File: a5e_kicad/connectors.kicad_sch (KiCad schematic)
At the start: 0 parts

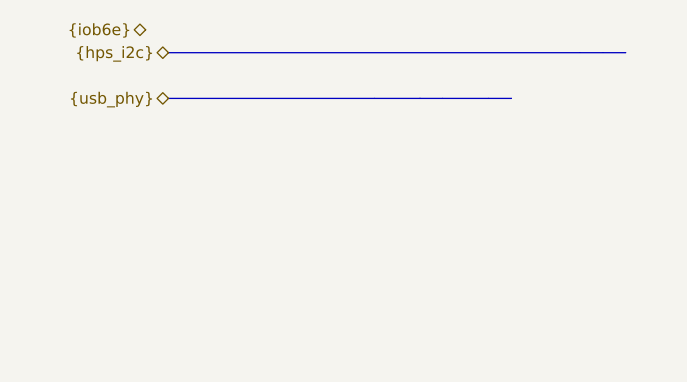
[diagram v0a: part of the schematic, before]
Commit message: Remove unused USB leftovers
USB is not used on this board.
- HPS sheet: remove the {hps_usb} ULPI bus, labels and wires; the 12
  U7 USB0 pins get no-connect flags
- Connectors sheet: remove the {usb_phy} hierarchical label and bus
- Clock sheet: remove the unused clk4 (USB 24 MHz) outputs and note
- Top-level: remove the {hps_usb}, {usb_phy}, clk4_P/clk4_N sheet pins
  and the usb_clk24 net

Netlist compared before/after: only the 12 USB pin nets changed (now
unconnected). ERC 542 -> 522.
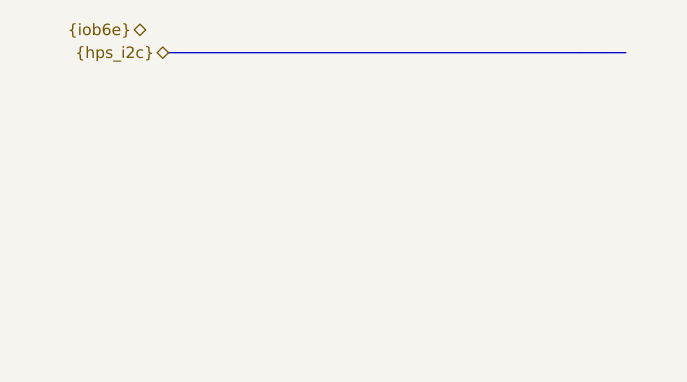
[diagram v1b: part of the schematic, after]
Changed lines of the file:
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@@
-	(bus
-		(pts
-			(xy 30.48 22.86) (xy 53.34 22.86)
-		)
-		(stroke
-			(width 0)
-			(type default)
-		)
-	)
 	(bus
 		(pts
@@
 	(bus
 		(pts
-			(xy 53.34 22.86) (xy 58.42 22.86)
-		)
-		(stroke
-			(width 0)
-			(type default)
-		)
-	)
-	(bus
-		(pts
 			(xy 35.56 134.62) (xy 35.56 193.04)
 		)
@@
 	(bus
 		(pts
-			(xy 60.96 22.86) (xy 66.04 22.86)
-		)
-		(stroke
-			(width 0)
-			(type default)
-		)
-	)
-	(bus
-		(pts
 			(xy 71.12 193.04) (xy 73.66 193.04)
 		)
@@
 	(bus
 		(pts
-			(xy 66.04 22.86) (xy 68.58 22.86)
-		)
-		(stroke
-			(width 0)
-			(type default)
-		)
-	)
-	(bus
-		(pts
 			(xy 266.7 129.54) (xy 269.24 129.54)
 		)
@@
 		(pts
 			(xy 93.98 193.04) (xy 96.52 193.04)
-		)
-		(stroke
-			(width 0)
-			(type default)
-		)
-	)
-	(bus
-		(pts
-			(xy 58.42 22.86) (xy 60.96 22.86)
 		)
 		(stroke
@@
 		(effects
 			(font
-				(size 1.27 1.27)
-			)
-			(justify right)
-		)
-	)
-	(hierarchical_label "{usb_phy}"
-		(shape bidirectional)
-		(at 30.48 22.86 180)
-		(effects
-			(font

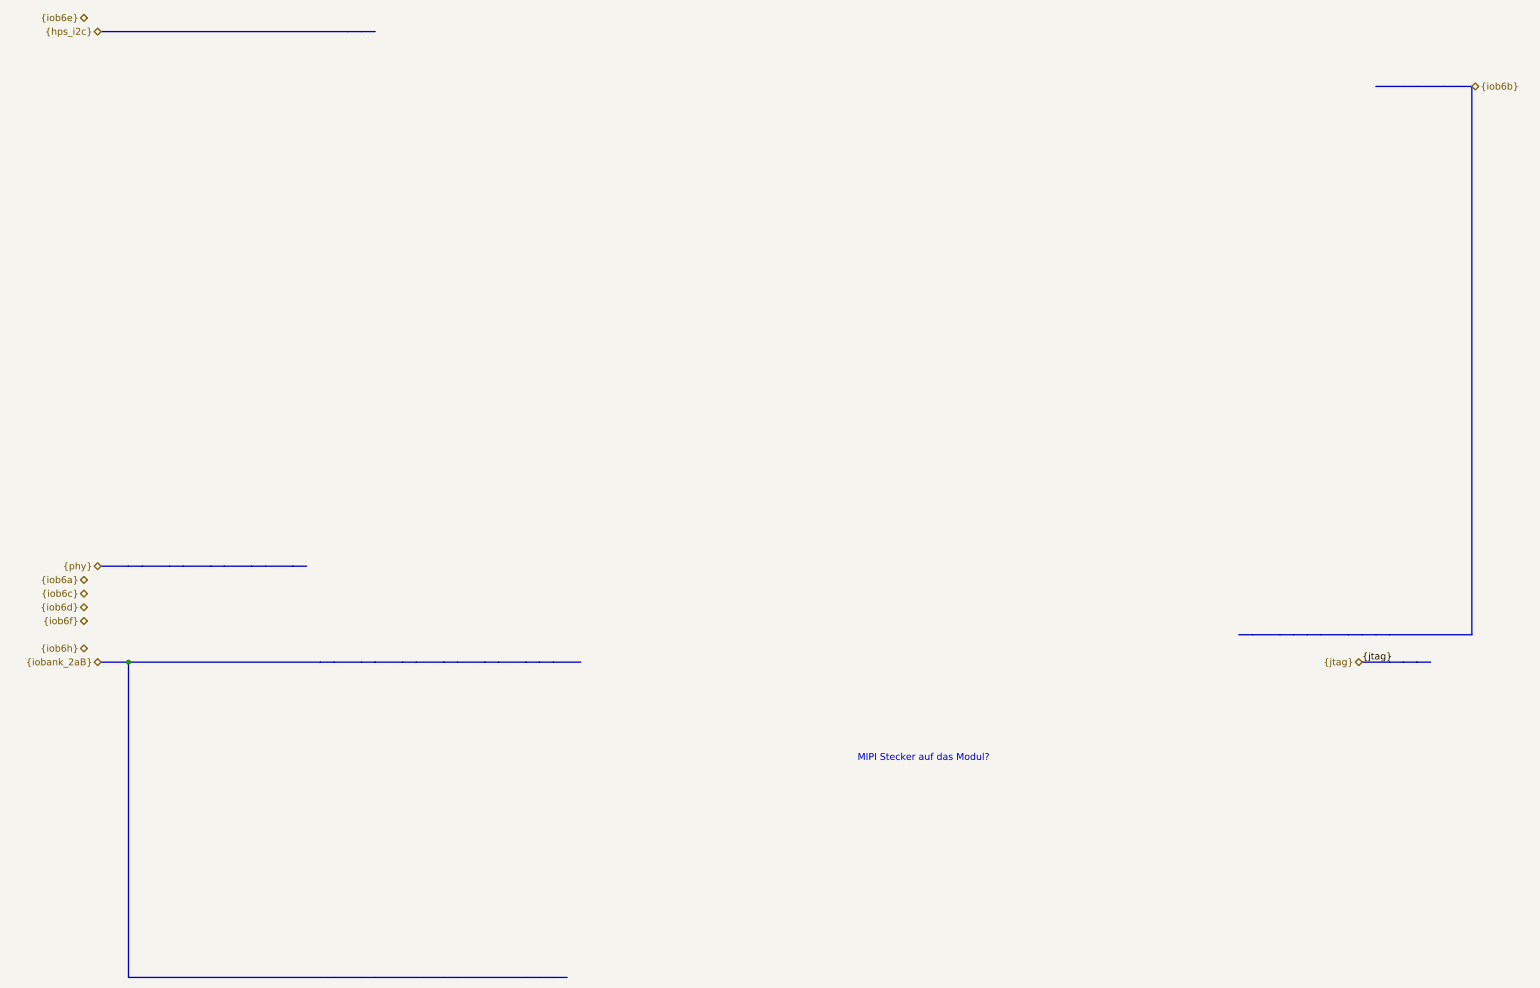
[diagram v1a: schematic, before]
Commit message: Update PCB from schematic
Sync net names after the P1/P2/USB cleanup (schematic parity 142 -> 0).
KiCad also dropped the empty leftover buses on the connectors sheet and
re-serialized instance data. Netlist unchanged.
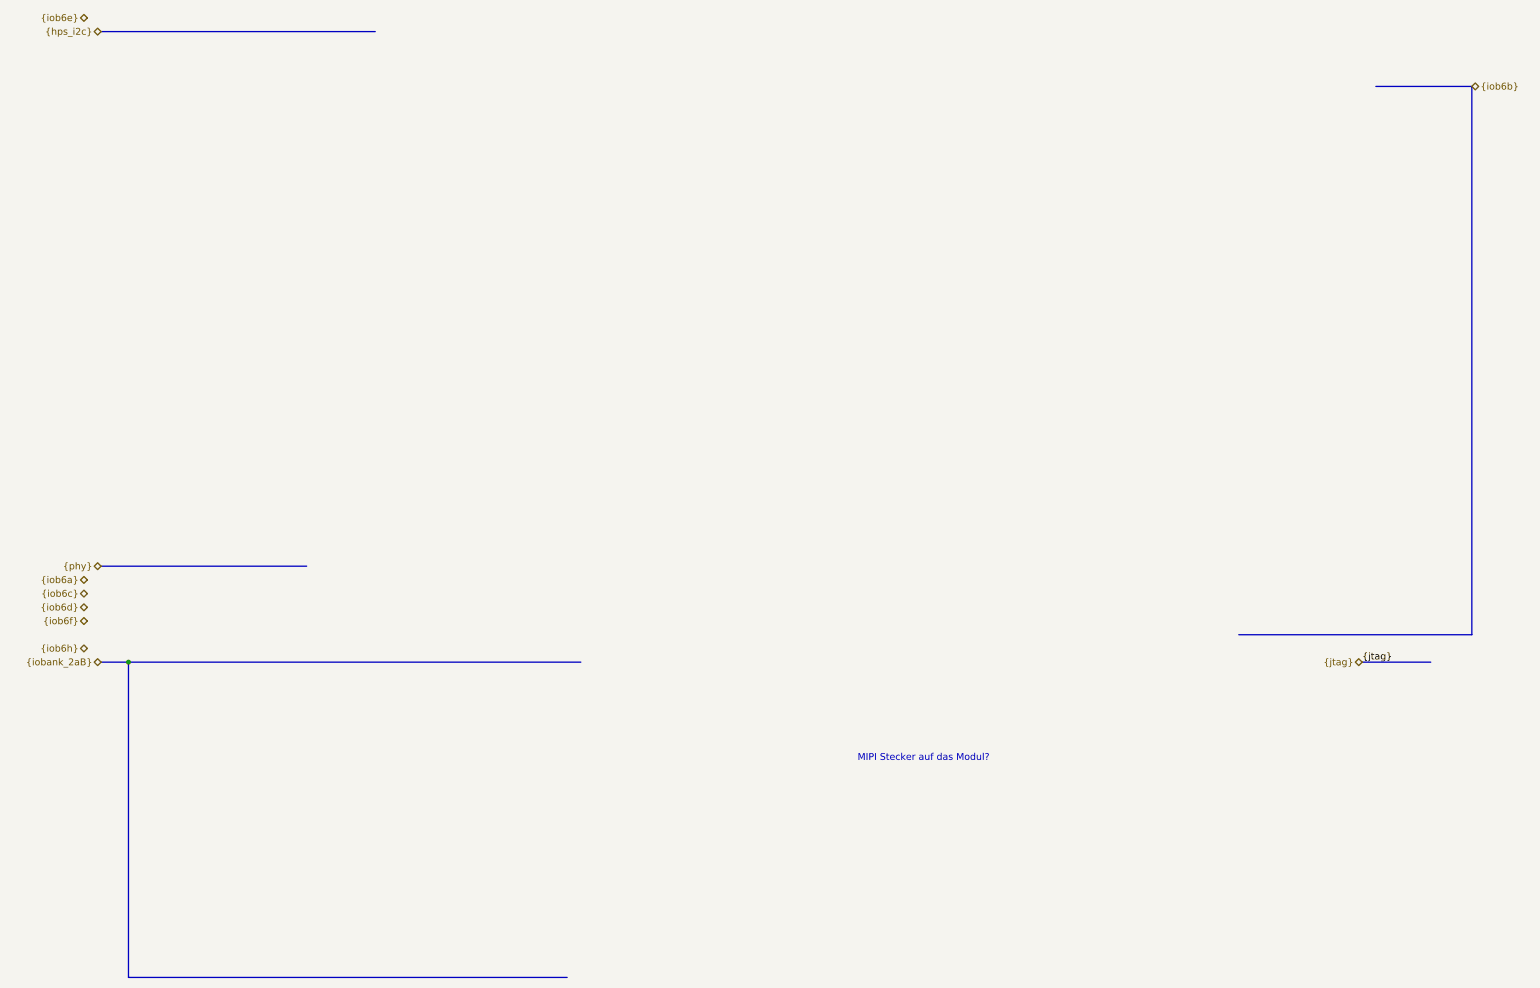
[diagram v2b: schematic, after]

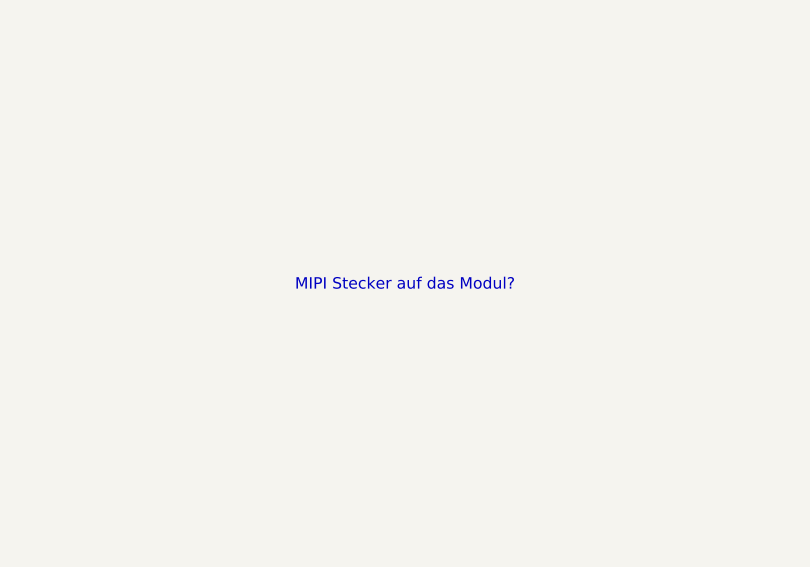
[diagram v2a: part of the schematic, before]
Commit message: Schematic reorg step 1: remove dangling stubs and stale notes, correct notes, fill title blocks
Netlist: 0 renamed, 0 connectivity diffs; DRC parity 0. ERC 315 -> 242.
Plan refreshed for the eMMC, RTL8211FDI, TPS548A28 and the tuned LPDDR4 (IOBANK 3 sheet name kept).
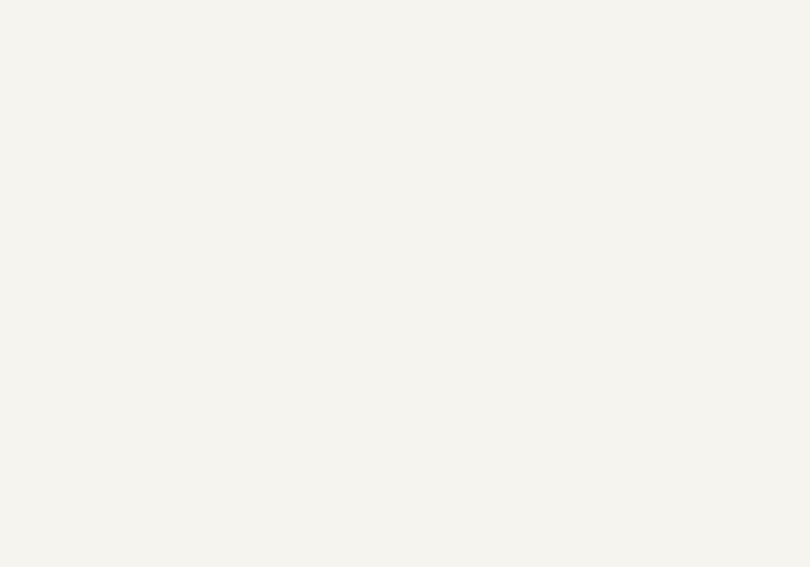
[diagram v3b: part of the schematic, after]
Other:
- note removed: "MIPI Stecker auf das Modul?"
- title: (none) -> FPGA I/O header buses
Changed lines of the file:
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@@
 	(paper "A4")
 	(title_block
-		(rev "0.1")
-	)
-	(text "MIPI Stecker auf das Modul? "
-		(exclude_from_sim no)
-		(at 182.88 152.4 0)
-		(effects
-			(font
-				(size 1.27 1.27)
-				(color 255 0 34 1)
-			)
-		)
+		(title "FPGA I/O header buses")
+		(rev "${REVISION}")
+		(comment 1 "${BOARD}")
 	)
 	(junction

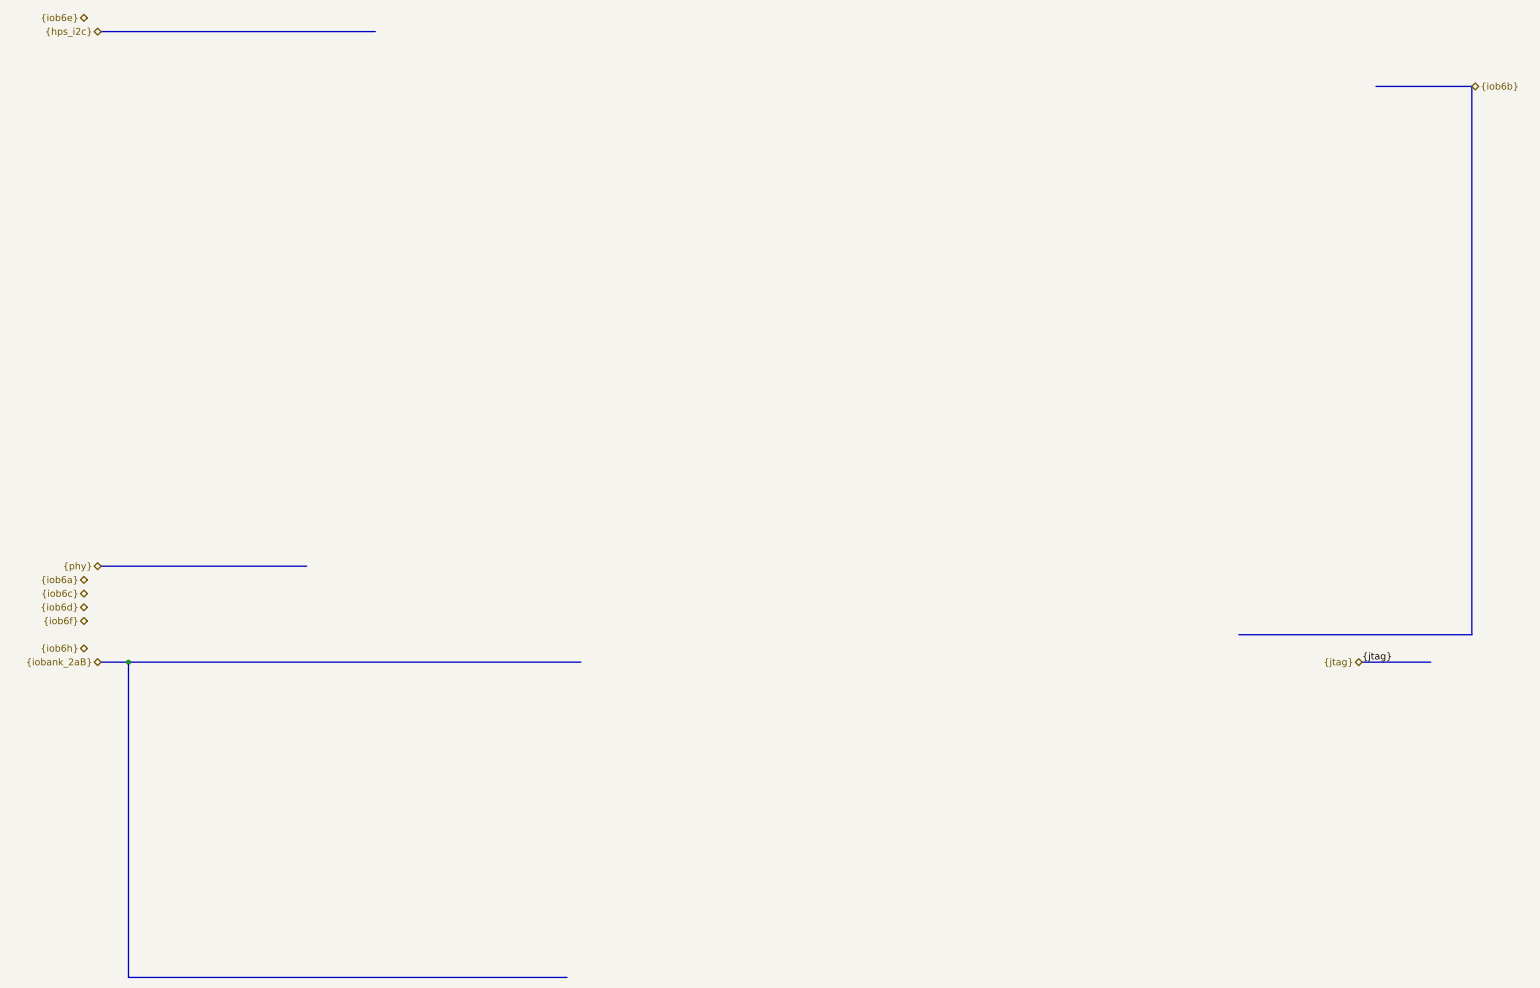
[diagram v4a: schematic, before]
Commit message: Schematic reorg step 5b: headers J3/J5 and pull-downs onto the Connectors sheet
- J3, J5, RN1-RN7 moved from the root to connectors.kicad_sch (same UUIDs);
  pins connect by label name to the sheet's bus labels
- New sheet pins {iob6g} and {ad_ch}; root bank buses are straight lines to the
  Connectors sheet; old bus tree, bus entries and stray junctions removed
- PCB: footprints re-linked, 15 nets renamed (iob6g*, ADC SPI/mux nets)

Netdiff: 15 renamed, 0 connectivity diffs. ERC 183 -> 180. DRC parity 0.
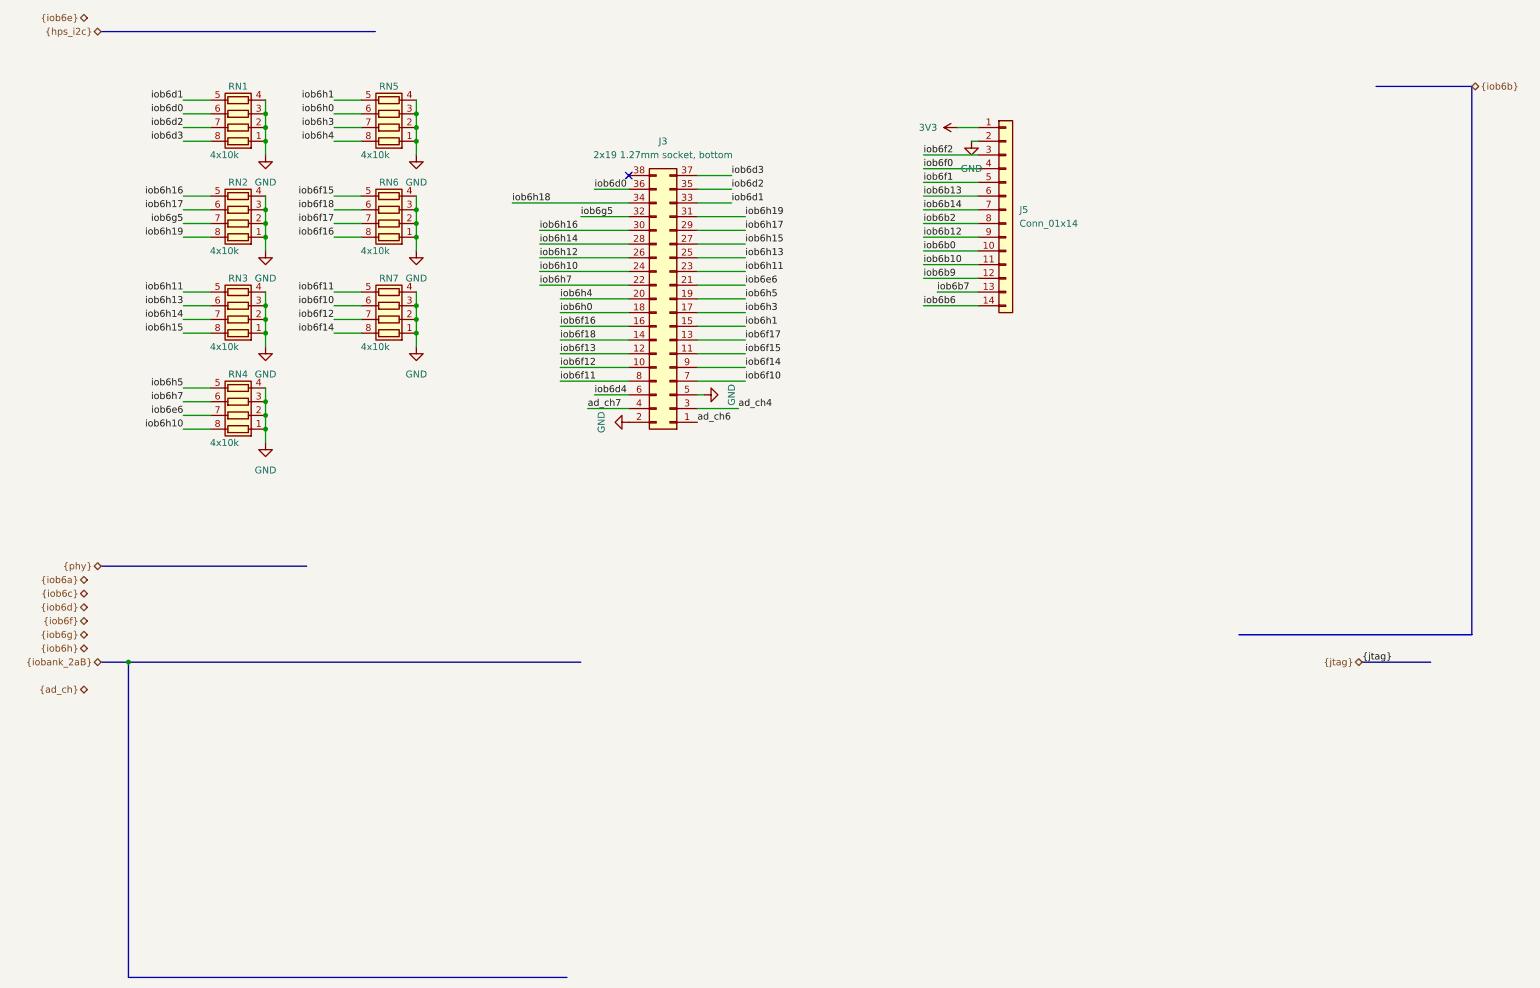
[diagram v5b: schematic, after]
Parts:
- added J3: 2x19 1.27mm socket, bottom, Connector_PinSocket_1.27mm:PinSocket_2x19_P1.27mm_Vertical, symbol Connector_Generic:Conn_02x19_Odd_Even
- added J5: Conn_01x14, Connector_PinHeader_2.54mm:PinHeader_1x14_P2.54mm_Vertical, symbol Connector_Generic:Conn_01x14
- added RN1, RN2, RN3, RN4, RN5, RN6, RN7: 4x10k, Resistor_SMD:R_Array_Convex_4x0402, symbol Device:R_Pack04
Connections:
- new net 3V3: J5.1 (Pin_1)
- new net GND: J3.2 (Pin_2), J3.5 (Pin_5), J5.2 (Pin_2), RN1.1 (R1.1), RN1.2 (R2.1), RN1.3 (R3.1), RN1.4 (R4.1), RN2.1 (R1.1), RN2.2 (R2.1), RN2.3 (R3.1), RN2.4 (R4.1), RN3.1 (R1.1), RN3.2 (R2.1), RN3.3 (R3.1), RN3.4 (R4.1), RN4.1 (R1.1), RN4.2 (R2.1), RN4.3 (R3.1), RN4.4 (R4.1), RN5.1 (R1.1), RN5.2 (R2.1), RN5.3 (R3.1), RN5.4 (R4.1), RN6.1 (R1.1), RN6.2 (R2.1), RN6.3 (R3.1), RN6.4 (R4.1), RN7.1 (R1.1), RN7.2 (R2.1), RN7.3 (R3.1), RN7.4 (R4.1)
- new net ad_ch4: J3.3 (Pin_3)
- new net ad_ch6: J3.1 (Pin_1)
- new net ad_ch7: J3.4 (Pin_4)
- new net iob6b0: J5.10 (Pin_10)
- new net iob6b10: J5.11 (Pin_11)
- new net iob6b12: J5.9 (Pin_9)
- new net iob6b13: J5.6 (Pin_6)
- new net iob6b14: J5.7 (Pin_7)
- new net iob6b2: J5.8 (Pin_8)
- new net iob6b6: J5.14 (Pin_14)
- new net iob6b7: J5.13 (Pin_13)
- new net iob6b9: J5.12 (Pin_12)
- new net iob6d0: J3.36 (Pin_36), RN1.6 (R3.2)
- new net iob6d1: J3.33 (Pin_33), RN1.5 (R4.2)
- new net iob6d2: J3.35 (Pin_35), RN1.7 (R2.2)
- new net iob6d3: J3.37 (Pin_37), RN1.8 (R1.2)
- new net iob6d4: J3.6 (Pin_6)
- new net iob6e6: J3.21 (Pin_21), RN4.7 (R2.2)
- new net iob6f0: J5.4 (Pin_4)
- new net iob6f1: J5.5 (Pin_5)
- new net iob6f10: J3.7 (Pin_7), RN7.6 (R3.2)
- new net iob6f11: J3.8 (Pin_8), RN7.5 (R4.2)
- new net iob6f12: J3.10 (Pin_10), RN7.7 (R2.2)
- new net iob6f13: J3.12 (Pin_12)
- new net iob6f14: J3.9 (Pin_9), RN7.8 (R1.2)
- new net iob6f15: J3.11 (Pin_11), RN6.5 (R4.2)
- new net iob6f16: J3.16 (Pin_16), RN6.8 (R1.2)
- new net iob6f17: J3.13 (Pin_13), RN6.7 (R2.2)
- new net iob6f18: J3.14 (Pin_14), RN6.6 (R3.2)
- new net iob6f2: J5.3 (Pin_3)
- new net iob6g5: J3.32 (Pin_32), RN2.7 (R2.2)
- new net iob6h0: J3.18 (Pin_18), RN5.6 (R3.2)
- new net iob6h1: J3.15 (Pin_15), RN5.5 (R4.2)
- new net iob6h10: J3.24 (Pin_24), RN4.8 (R1.2)
- new net iob6h11: J3.23 (Pin_23), RN3.5 (R4.2)
- new net iob6h12: J3.26 (Pin_26)
- new net iob6h13: J3.25 (Pin_25), RN3.6 (R3.2)
- new net iob6h14: J3.28 (Pin_28), RN3.7 (R2.2)
- new net iob6h15: J3.27 (Pin_27), RN3.8 (R1.2)
- new net iob6h16: J3.30 (Pin_30), RN2.5 (R4.2)
- new net iob6h17: J3.29 (Pin_29), RN2.6 (R3.2)
- new net iob6h18: J3.34 (Pin_34)
- new net iob6h19: J3.31 (Pin_31), RN2.8 (R1.2)
- new net iob6h3: J3.17 (Pin_17), RN5.7 (R2.2)
- new net iob6h4: J3.20 (Pin_20), RN5.8 (R1.2)
- new net iob6h5: J3.19 (Pin_19), RN4.5 (R4.2)
- new net iob6h7: J3.22 (Pin_22), RN4.6 (R3.2)
- no-connect marks 0 -> 1
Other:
- title: FPGA I/O header buses -> FPGA I/O headers J3 / J5, 10k pull-downs

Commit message: Schematic reorg step 7: no global labels, NC flags on unused U7 pins
- hps_uart0_tx/rx, eth_rst_n, phy_rst_n, fpga_led: global labels replaced by
  sheet pins; eth_led_g_n is a local label
- HyperBus labels/bus, the HPS {hps_i2c} bus and the pwr_scl/pwr_sda wiring
  removed (nothing behind them)
- 118 U7 pins that only had a net label: label, stub and bus entry removed,
  no-connect flag added
- Bank 3A notes restacked
- PCB: 124 nets renamed (118 to unconnected-(U7...))

Netdiff: 124 renamed, 0 connectivity diffs. ERC 148 -> 21. DRC parity 0.
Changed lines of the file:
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@@
-	(bus
-		(pts
-			(xy 30.48 17.78) (xy 81.28 17.78)
-		)
-		(stroke
-			(width 0)
-			(type default)
-		)
-	)
 	(bus
 		(pts
@@
 		)
 	)
-	(hierarchical_label "{hps_i2c}"
-		(shape bidirectional)
-		(at 30.48 17.78 180)
-		(effects
-			(font
-				(size 1.27 1.27)
-			)
-			(justify right)
-		)
-	)
